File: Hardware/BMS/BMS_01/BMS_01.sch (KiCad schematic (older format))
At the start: 3 parts

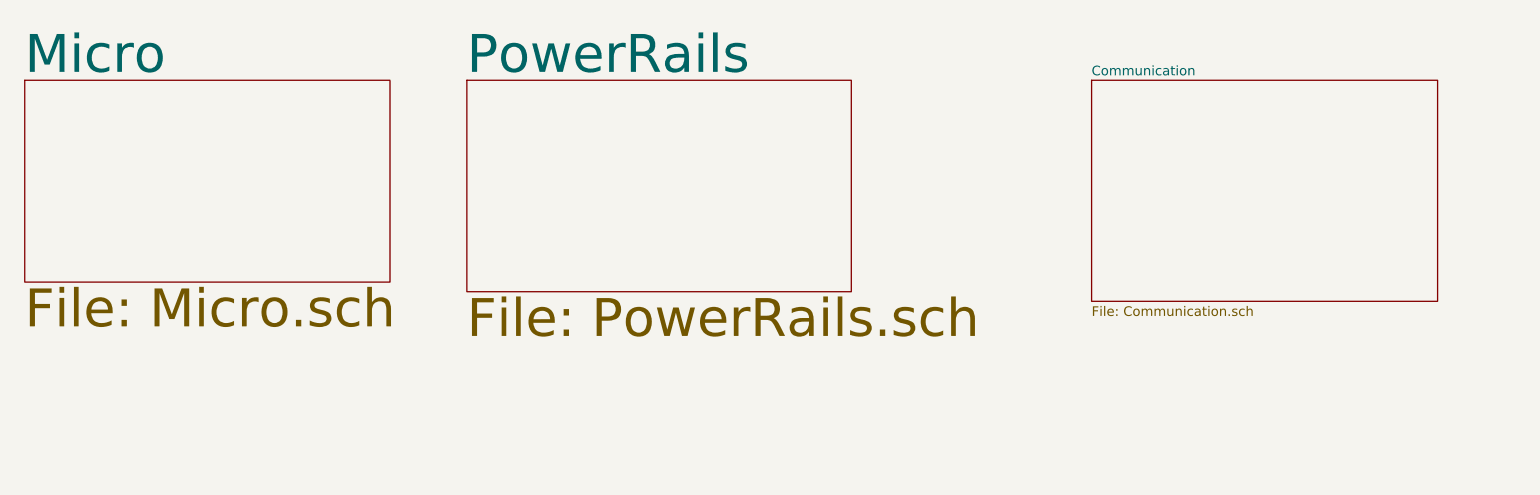
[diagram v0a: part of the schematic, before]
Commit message: Updated DCDC schematic with footprints. Moving onto BMS as higher priority. Footprints added, 5V regulator updated
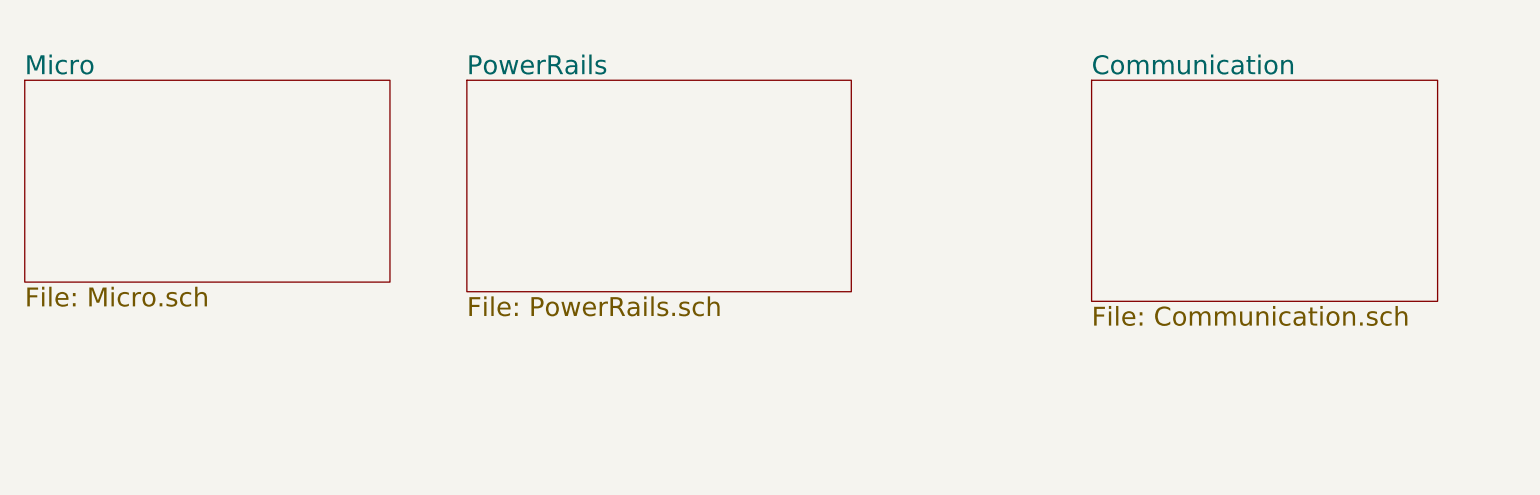
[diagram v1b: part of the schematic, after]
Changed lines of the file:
@@
 S 1100 750  1900 1050
 U 5AAB4D1F
-F0 "Micro" 197
-F1 "Micro.sch" 197
+F0 "Micro" 98
+F1 "Micro.sch" 98
 $EndSheet
 $Sheet
 S 3400 750  2000 1100
 U 5AAC0444
-F0 "PowerRails" 197
-F1 "PowerRails.sch" 197
+F0 "PowerRails" 98
+F1 "PowerRails.sch" 98
 $EndSheet
 $Comp
@@
 S 6650 750  1800 1150
 U 5AC3D661
-F0 "Communication" 50
-F1 "Communication.sch" 50
+F0 "Communication" 98
+F1 "Communication.sch" 98
 $EndSheet
 $EndSCHEMATC

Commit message: Added foorprints for BMS schematics
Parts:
- D1, D2, D3: footprint (none) -> Diodes_SMD:D_SOD-123F
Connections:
- wire segments 6 -> 22
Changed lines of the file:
@@
 $Descr A4 11693 8268
 encoding utf-8
-Sheet 1 30
+Sheet 1 52
 Title ""
 Date ""
@@
 F1 "PowerRails.sch" 98
 $EndSheet
-$Comp
-L device:D D1
-U 1 1 5AC2C048
-P 3050 4750
-F 0 "D1" H 3050 4534 50  0000 C CNN
-F 1 "D" H 3050 4625 50  0000 C CNN
-F 2 "" H 3050 4750 50  0001 C CNN
-F 3 "" H 3050 4750 50  0001 C CNN
-	1    3050 4750
-	-1   0    0    1
-$EndComp
 Wire Wire Line
 	2750 4450 3300 4450
@@
 	3600 4450 3700 4450
 $Comp
-L device:D D2
-U 1 1 5AC2C068
-P 3250 4650
-F 0 "D2" H 3250 4434 50  0000 C CNN
-F 1 "D" H 3250 4525 50  0000 C CNN
-F 2 "" H 3250 4650 50  0001 C CNN
-F 3 "" H 3250 4650 50  0001 C CNN
-	1    3250 4650
-	-1   0    0    1
-$EndComp
-$Comp
 L device:D D3
 U 1 1 5AC2BFD0
@@
 F 0 "D3" H 3450 4234 50  0000 C CNN
 F 1 "D" H 3450 4325 50  0000 C CNN
-F 2 "" H 3450 4450 50  0001 C CNN
-F 3 "" H 3450 4450 50  0001 C CNN
+F 2 "Diodes_SMD:D_SOD-123F" H 3450 4450 50  0001 C CNN
+F 3 "https://www.onsemi.com/pub/Collateral/RS1AFA-D.PDF" H 3450 4450 50  0001 C CNN
 	1    3450 4450
 	-1   0    0    1
@@
 F1 "Communication.sch" 98
 $EndSheet
+$Sheet
+S 1100 2050 1900 900
+U 5B56E059
+F0 "TempSensors" 98
+F1 "TempSensors.sch" 98
+$EndSheet
+Wire Wire Line
+	5350 5000 5650 5000
+Wire Wire Line
+	5650 5000 5650 5100
+Wire Wire Line
+	5650 5100 5350 5100
+Wire Wire Line
+	2750 5000 2850 5000
+Wire Wire Line
+	2850 5000 2850 7500
+Wire Wire Line
+	2850 7500 900  7500
+Wire Wire Line
+	900  7500 900  6200
+Wire Wire Line
+	900  6200 1050 6200
+Wire Wire Line
+	2750 5100 2900 5100
+Wire Wire Line
+	2900 5100 2900 4900
+Wire Wire Line
+	2900 4900 2750 4900
+$Comp
+L device:D D2
+U 1 1 5B634C12
+P 3250 4650
+F 0 "D2" H 3250 4434 50  0000 C CNN
+F 1 "D" H 3250 4525 50  0000 C CNN
+F 2 "Diodes_SMD:D_SOD-123F" H 3250 4650 50  0001 C CNN
+F 3 "https://www.onsemi.com/pub/Collateral/RS1AFA-D.PDF" H 3250 4650 50  0001 C CNN
+	1    3250 4650
+	-1   0    0    1
+$EndComp
+$Comp
+L device:D D1
+U 1 1 5B634C32
+P 3050 4750
+F 0 "D1" H 3050 4534 50  0000 C CNN
+F 1 "D" H 3050 4625 50  0000 C CNN
+F 2 "Diodes_SMD:D_SOD-123F" H 3050 4750 50  0001 C CNN
+F 3 "https://www.onsemi.com/pub/Collateral/RS1AFA-D.PDF" H 3050 4750 50  0001 C CNN
+	1    3050 4750
+	-1   0    0    1
+$EndComp
+Wire Wire Line
+	5350 4900 5700 4900
+Wire Wire Line
+	5700 4900 5700 7500
+Wire Wire Line
+	5700 7500 3550 7500
+Wire Wire Line
+	3550 7500 3550 6200
+Wire Wire Line
+	3550 6200 3700 6200
+$Sheet
+S 3400 2150 1950 1000
+U 5B64EF74
+F0 "Connectors" 98
+F1 "Connectors.sch" 98
+$EndSheet
 $EndSCHEMATC

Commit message: BMS Connectors
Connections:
- net labels added: BANK_01, BANK_02, BANK_03, BANK_04, BANK_05, BANK_06, BANK_07, BANK_08, BANK_09, BANK_10, BANK_11, BANK_12, BANK_13, BANK_14, BANK_15, BANK_16, BANK_17, BANK_18, BANK_19, BANK_20, BANK_21, BANK_22, BANK_23, BANK_24, GND
- wire segments 22 -> 41

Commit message: Too much stuff to list
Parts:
- removed D1, D2, D3: D, Diodes_SMD:D_SOD-123F, symbol device:D
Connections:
- net labels removed: BANK_01, BANK_02, BANK_03, BANK_04, BANK_05, BANK_06, BANK_07, BANK_08, BANK_09, BANK_10, BANK_11, BANK_12, BANK_13, BANK_14, BANK_15, BANK_16, BANK_17, BANK_18, BANK_19, BANK_20, BANK_21, BANK_22, BANK_23, BANK_24, GND
- wire segments 41 -> 0
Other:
- note added: "24 Series Connections\n90V Pack Nominal\nResistive Pack Balancing\nCurrent Transducer\n24 external NTCs"
- note added: "Battery Management System (BMS)"

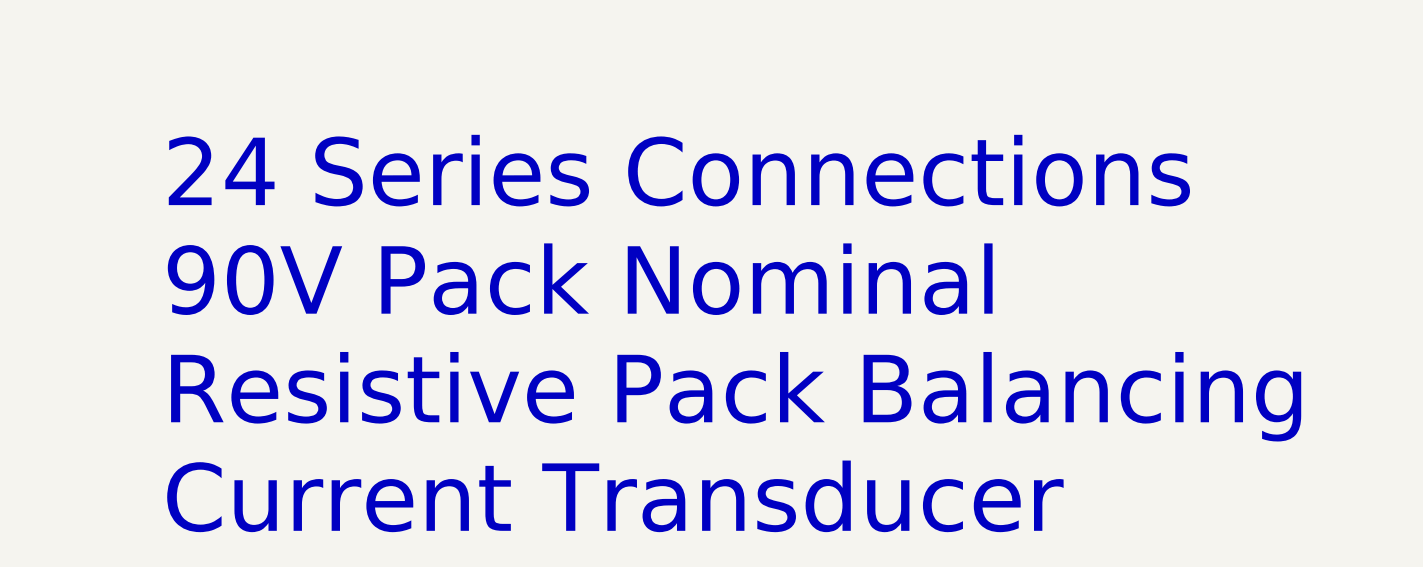
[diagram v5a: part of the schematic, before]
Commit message: BMS controller. Lots of new FW including bootloaders
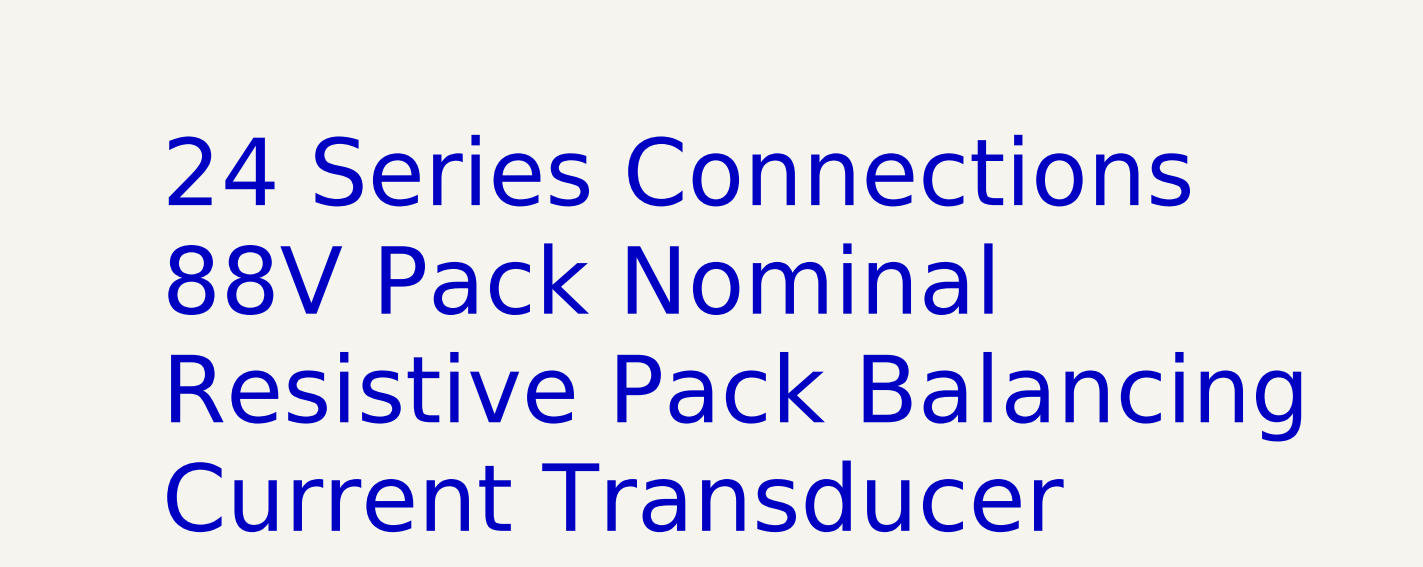
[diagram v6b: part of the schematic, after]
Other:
- note added: "24 Series Connections\n88V Pack Nominal\nResistive Pack Balancing\nCurrent Transducer\n24 external NTCs"
- note removed: "24 Series Connections\n90V Pack Nominal\nResistive Pack Balancing\nCurrent Transducer\n24 external NTCs"
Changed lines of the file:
@@
 $Descr A4 11693 8268
 encoding utf-8
-Sheet 1 59
+Sheet 1 61
 Title ""
 Date ""
@@
 Battery Management System (BMS)
 Text Notes 1250 4300 0    295  ~ 0
-24 Series Connections\n90V Pack Nominal\nResistive Pack Balancing\nCurrent Transducer\n24 external NTCs
+24 Series Connections\n88V Pack Nominal\nResistive Pack Balancing\nCurrent Transducer\n24 external NTCs
 $EndSCHEMATC
